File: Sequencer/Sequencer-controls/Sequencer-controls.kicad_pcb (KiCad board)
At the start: 2 copper layers, 163.5 x 105.5 mm, 97 parts, among them SW1 SW_Push_DPDT, SW10 SW_SPDT, SW11 SW_SPDT, SW12 SW_SPDT, SW13 SW_SPDT, SW14 SW_SPDT, SW15 SW_SPDT, SW16 SW_SPDT, SW17 SW_SPDT, SW18 SW_SPDT, SW19 SW_SPDT, SW4 SW_SPDT, SW5 SW_SPDT, SW6 SW_SPDT, SW7 SW_SPDT, SW8 SW_SPDT, SW9 SW_SPDT

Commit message: just playing around
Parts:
- D  : renamed from D3
- moved D   23.8 mm to (9.00, 9.00), turned to -90 degrees
- moved D2 23.8 mm to (3.50, 20.0)
- moved RV_FINE1 23.8 mm to (9.00, 35.0)
- moved SW4 23.8 mm to (9.00, 20.0)
- moved RV_COARSE1 23.7 mm to (9.00, 50.0)
- moved RV_COARSE2 23.4 mm to (23.0, 50.0)
- moved D5 22.2 mm to (25.0, 9.00), turned to -90 degrees
- moved D4 22.0 mm to (19.5, 20.0)
- moved RV_FINE2 22.0 mm to (25.0, 35.0)
- moved SW5 22.0 mm to (25.0, 20.0)
- moved D7 20.6 mm to (41.0, 9.00), turned to -90 degrees
- moved D6 20.2 mm to (35.5, 20.0)
- moved RV_FINE3 20.2 mm to (41.0, 35.0)
- moved SW6 20.2 mm to (41.0, 20.0)
- moved RV_COARSE3 20.2 mm to (41.0, 50.0)
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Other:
- board size 163.5 x 105.5 mm -> 180 x 116.5 mm

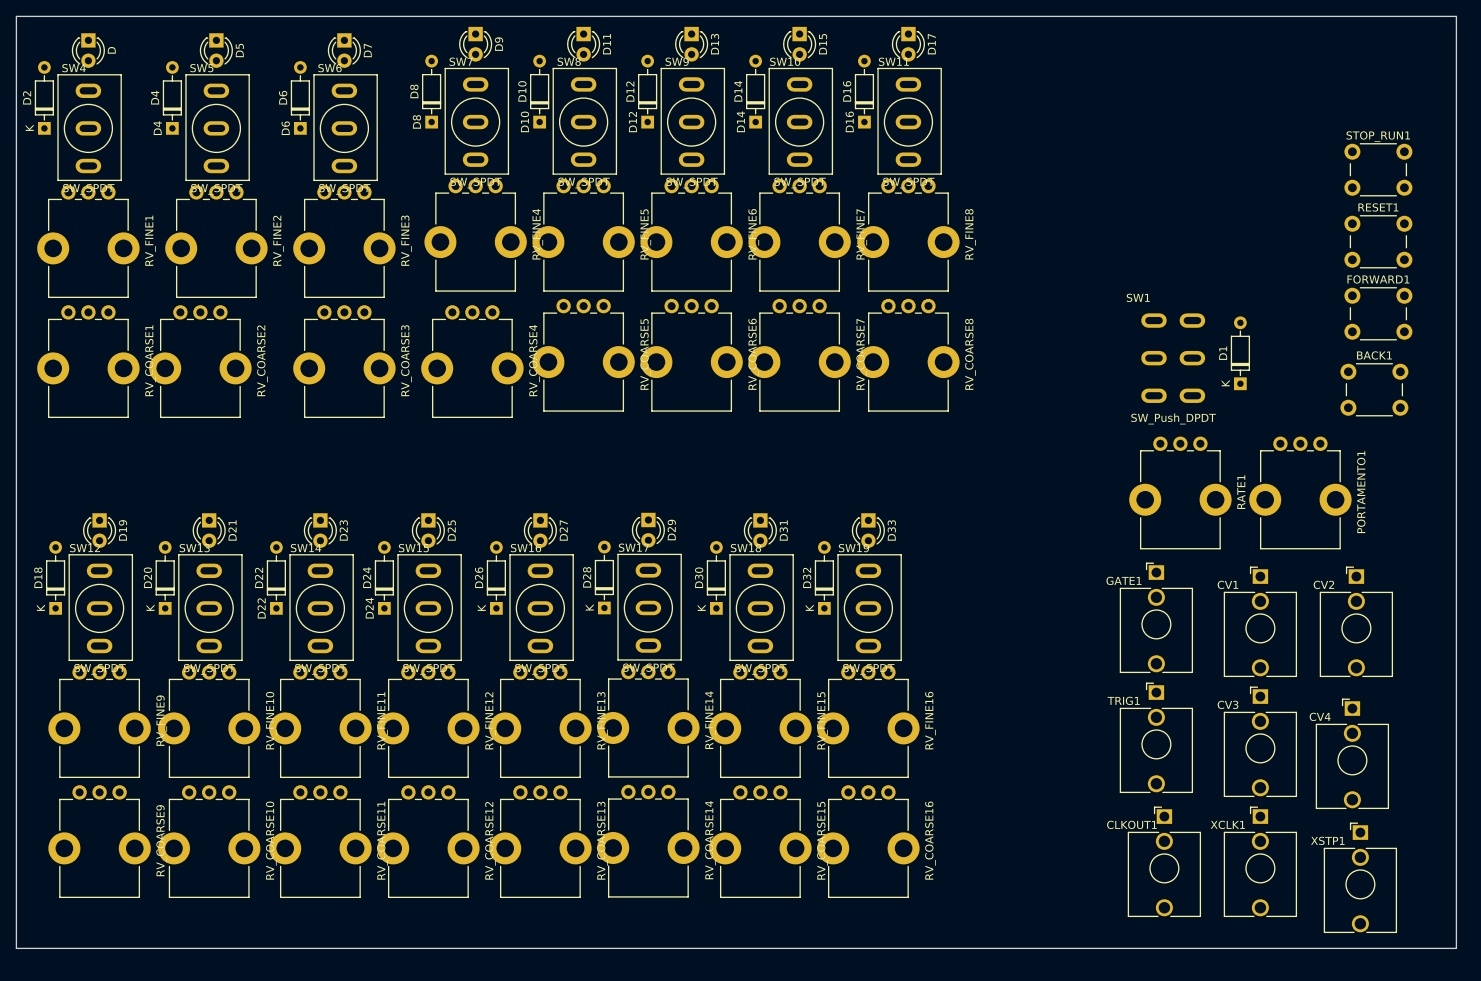
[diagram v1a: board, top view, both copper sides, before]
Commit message: adding connectors to sequencer
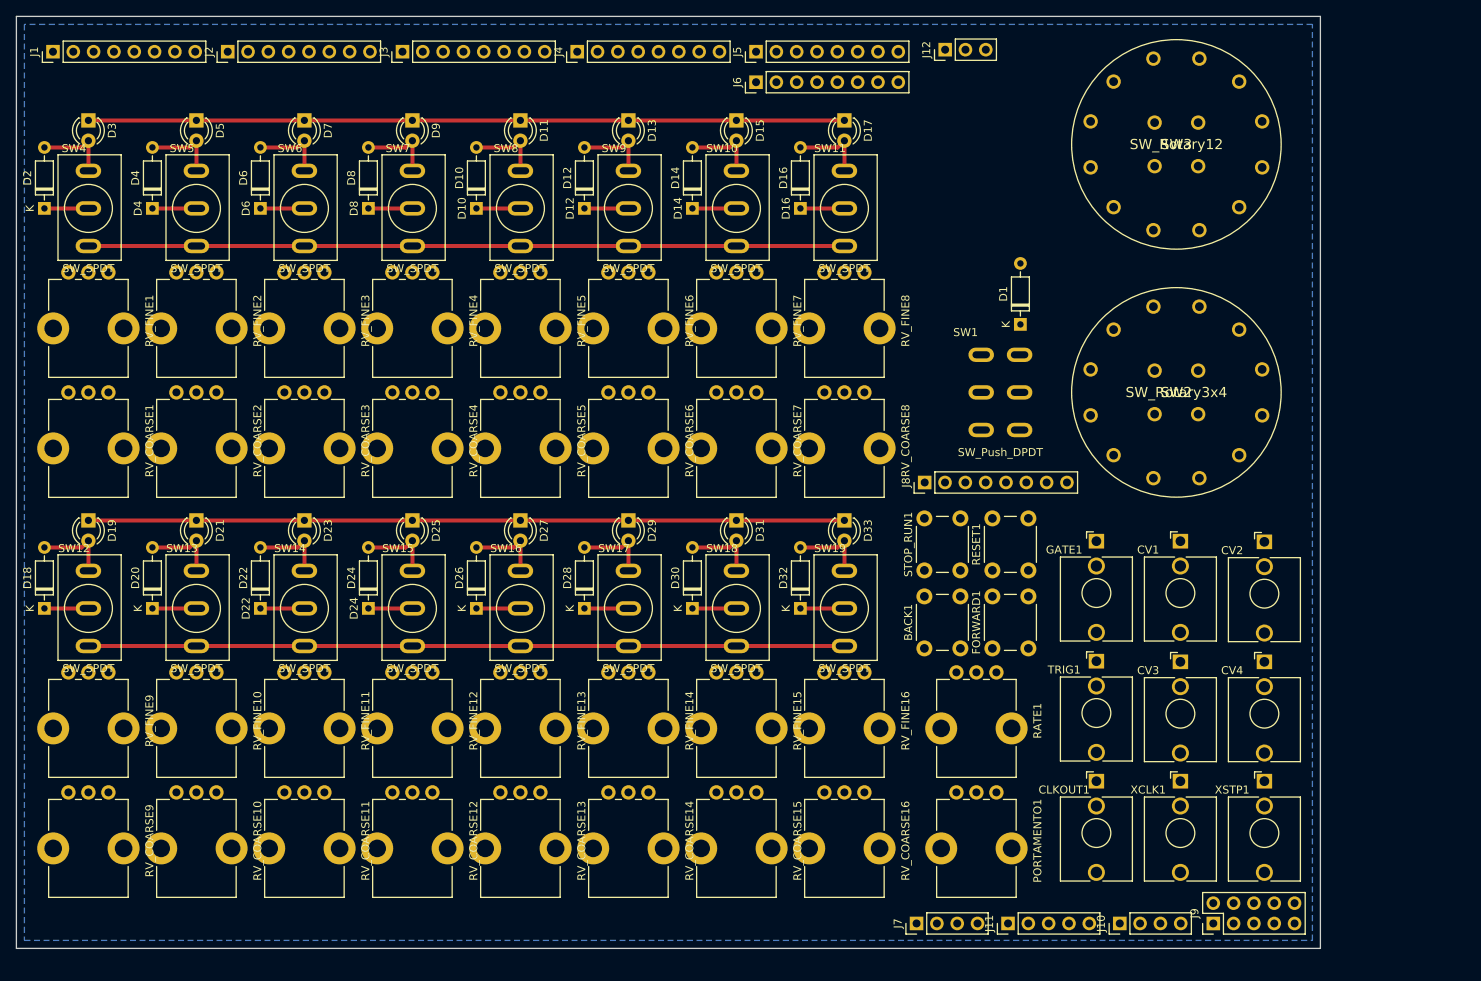
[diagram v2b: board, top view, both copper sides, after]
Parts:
- added J1: Conn_01x08, Connector_PinHeader_2.54mm:PinHeader_1x08_P2.54mm_Vertical, F.Cu at (4.57, 10.4)
- added J10: Conn_01x04, Connector_PinHeader_2.54mm:PinHeader_1x04_P2.54mm_Vertical, F.Cu at (137.9, 119.4)
- added J11: Conn_01x05, Connector_PinHeader_2.54mm:PinHeader_1x05_P2.54mm_Vertical, F.Cu at (124.0, 119.4)
- added J12: Conn_01x03, Connector_PinHeader_2.54mm:PinHeader_1x03_P2.54mm_Vertical, F.Cu at (116.1, 10.2)
- added J2: Conn_01x08, Connector_PinHeader_2.54mm:PinHeader_1x08_P2.54mm_Vertical, F.Cu at (26.4, 10.4)
- added J3: Conn_01x08, Connector_PinHeader_2.54mm:PinHeader_1x08_P2.54mm_Vertical, F.Cu at (48.3, 10.4)
- added J4: Conn_01x08, Connector_PinHeader_2.54mm:PinHeader_1x08_P2.54mm_Vertical, F.Cu at (70.1, 10.4)
- added J5: Conn_01x08, Connector_PinHeader_2.54mm:PinHeader_1x08_P2.54mm_Vertical, F.Cu at (92.5, 10.4)
- added J6: Conn_01x08, Connector_PinHeader_2.54mm:PinHeader_1x08_P2.54mm_Vertical, F.Cu at (92.5, 14.2)
- added J7: Conn_01x04, Connector_PinHeader_2.54mm:PinHeader_1x04_P2.54mm_Vertical, F.Cu at (112.5, 119.4)
- added J8: Conn_01x08, Connector_PinHeader_2.54mm:PinHeader_1x08_P2.54mm_Vertical, F.Cu at (113.5, 64.3)
- added J9: Conn_02x05_Counter_Clockwise, Connector_PinHeader_2.54mm:PinHeader_2x05_P2.54mm_Vertical, F.Cu at (149.6, 119.4)
- added SW2: SW_Rotary3x4, Library:rotary_switch_1P12T, F.Cu at (145.0, 53.0)
- added SW3: SW_Rotary12, Library:rotary_switch_1P12T, F.Cu at (145.0, 22.0)
- D3: renamed from D  
- moved STOP_RUN1 74.8 mm to (113.5, 75.2), turned to 90 degrees
- moved BACK1 63.3 mm to (113.5, 85.0), turned to 90 degrees
- moved FORWARD1 63.0 mm to (122.0, 85.0), turned to 90 degrees
- moved RESET1 62.5 mm to (122.0, 75.2), turned to 90 degrees
- moved PORTAMENTO1 59.5 mm to (120.0, 110.0)
- moved RATE1 38.3 mm to (120.0, 95.0)
- moved D1 28.5 mm to (125.5, 44.5)
- moved SW1 22.0 mm to (123.0, 53.0)
- moved XSTP1 13.6 mm to (156.0, 108.1)
- moved D16 13.4 mm to (98.0, 30.0)
- moved D17 13.4 mm to (103.5, 19.0)
- moved RV_COARSE8 13.4 mm to (103.5, 60.0)
- moved RV_FINE8 13.4 mm to (103.5, 45.0)
- moved SW11 13.4 mm to (103.5, 30.0)
- moved D8 13.4 mm to (44.0, 30.0)
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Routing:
- net GB: track 0.00 -> 189.0 mm
- net CBUS: track 0.00 -> 189.0 mm
- net S7: track 0.00 -> 9.61 mm
- net S5: track 0.00 -> 9.61 mm
- net S4: track 0.00 -> 9.61 mm
- net S3: track 0.00 -> 9.61 mm
- net S2: track 0.00 -> 9.61 mm
- net S1: track 0.00 -> 9.61 mm
- net S8: track 0.00 -> 9.61 mm
- net S6: track 0.00 -> 9.61 mm
- net S9: track 0.00 -> 9.61 mm
- net S10: track 0.00 -> 9.61 mm
- net S16: track 0.00 -> 9.61 mm
- net S15: track 0.00 -> 9.61 mm
- net S14: track 0.00 -> 9.61 mm
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- added copper zone on B.Cu, net GND
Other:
- board size 180 x 116.5 mm -> 163 x 116.5 mm

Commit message: Sequencer control fully routed
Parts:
- added H1: MountingHole_Pad, MountingHole:MountingHole_3.2mm_M3_Pad, F.Cu at (157.0, 37.5)
- added H2: MountingHole_Pad, MountingHole:MountingHole_3.2mm_M3_Pad, F.Cu at (105.0, 118.5)
- added H3: MountingHole_Pad, MountingHole:MountingHole_3.2mm_M3_Pad, F.Cu at (4.00, 118.6)
- SW2: footprint Library:rotary_switch_1P12T -> Library:rotary_switch_3P4T
- renumbered J8 to J10, J12 to J11, J9 to J12, J10 to J7, J11 to J8, J7 to J9
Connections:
- J12 pad 10: +12V -> -12V
- J12 pad 2: GND -> +12V
- J12 pad 5: -12V -> GND
- J12 pad 6: -12V -> GND
- J12 pad 9: GND -> -12V
- PORTAMENTO1 pad : (no net) -> GND
- RATE1 pad : (no net) -> GND
- RV_COARSE1 pad : (no net) -> GND
- RV_COARSE10 pad : (no net) -> GND
- RV_COARSE11 pad : (no net) -> GND
- RV_COARSE12 pad : (no net) -> GND
- RV_COARSE13 pad : (no net) -> GND
- RV_COARSE14 pad : (no net) -> GND
- RV_COARSE15 pad : (no net) -> GND
- RV_COARSE16 pad : (no net) -> GND
- RV_COARSE2 pad : (no net) -> GND
- RV_COARSE3 pad : (no net) -> GND
- RV_COARSE4 pad : (no net) -> GND
- RV_COARSE5 pad : (no net) -> GND
- RV_COARSE6 pad : (no net) -> GND
- RV_COARSE7 pad : (no net) -> GND
- RV_COARSE8 pad : (no net) -> GND
- RV_COARSE9 pad : (no net) -> GND
- RV_FINE1 pad : (no net) -> GND
- RV_FINE10 pad : (no net) -> GND
- RV_FINE11 pad : (no net) -> GND
- RV_FINE12 pad : (no net) -> GND
- RV_FINE13 pad : (no net) -> GND
- RV_FINE14 pad : (no net) -> GND
- RV_FINE15 pad : (no net) -> GND
- RV_FINE16 pad : (no net) -> GND
- RV_FINE2 pad : (no net) -> GND
- RV_FINE3 pad : (no net) -> GND
- RV_FINE4 pad : (no net) -> GND
- RV_FINE5 pad : (no net) -> GND
- RV_FINE6 pad : (no net) -> GND
- RV_FINE7 pad : (no net) -> GND
- RV_FINE8 pad : (no net) -> GND
- RV_FINE9 pad : (no net) -> GND
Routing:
- net VSRC: track 0.00 -> 520.5 mm
- net S9: track 9.61 -> 212.6 mm, vias 0 -> 1
- net S11: track 9.61 -> 192.0 mm, vias 0 -> 1
- net C11: track 0.00 -> 178.9 mm, vias 0 -> 1
- net S14: track 9.61 -> 184.0 mm
- net S12: track 9.61 -> 183.9 mm, vias 0 -> 1
- net S10: track 9.61 -> 178.4 mm, vias 0 -> 1
- net S13: track 9.61 -> 164.7 mm, vias 0 -> 2
- net C9: track 0.00 -> 146.3 mm
- net S15: track 9.61 -> 149.8 mm, vias 0 -> 1
- net F9: track 0.00 -> 128.3 mm
- net S4: track 9.61 -> 136.9 mm
- net C12: track 0.00 -> 117.9 mm, vias 0 -> 1
- net S5: track 9.61 -> 125.8 mm, vias 0 -> 1
- net S6: track 9.61 -> 120.7 mm, vias 0 -> 1
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- added copper zone on F.Cu, net GND
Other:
- board text added: "+12V"
- board text added: "-12V"
- board text added: "C1"
- board text added: "C10"
- board text added: "C11"
- board text added: "C12"
- board text added: "C13"
- board text added: "C14"
- board text added: "C15"
- board text added: "C16"
- board text added: "C2"
- board text added: "C3"
- board text added: "C4"
- board text added: "C5"
- board text added: "C6"
- board text added: "C7"
- board text added: "C8"
- board text added: "C9"
- board text added: "CBUS"
- board text added: "CLKOUT"
- board text added: "CV1"
- board text added: "CV2"
- board text added: "CV3"
- board text added: "F1"
- board text added: "F10"
- board text added: "F11"
- board text added: "F12"
- board text added: "F13"
- board text added: "F14"
- board text added: "F15"
- board text added: "F16"
- board text added: "F2"
- board text added: "F3"
- board text added: "F4"
- board text added: "F5"
- board text added: "F6"
- board text added: "F7"
- board text added: "F8"
- board text added: "F9"
- board text added: "GATE"
- board text added: "GB"
- board text added: "GND"
- board text added: "PORT_1_2"
- board text added: "PORT_3"
- board text added: "RATE_1_2"
- board text added: "RATE_3"
- board text added: "S1"
- board text added: "S16"
- board text added: "S8"
- board text added: "S9"
- board text added: "TRIG"
- board text added: "VSRC"
- board text added: "XCLK"
- board text added: "XSTP"

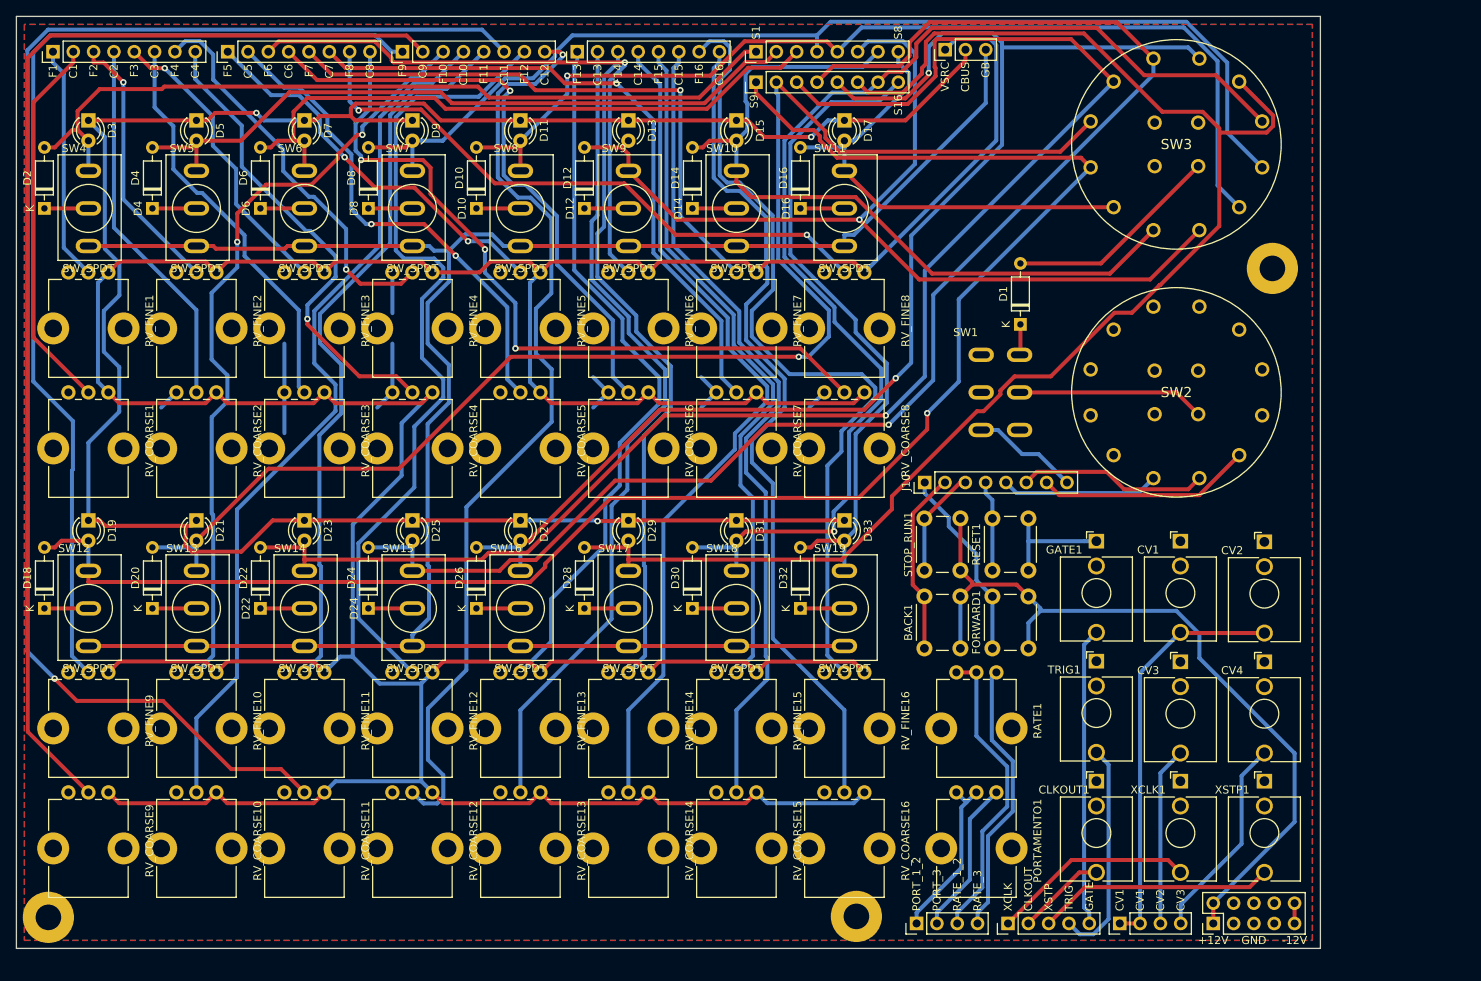
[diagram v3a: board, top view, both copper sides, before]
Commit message: moved to 4 layers
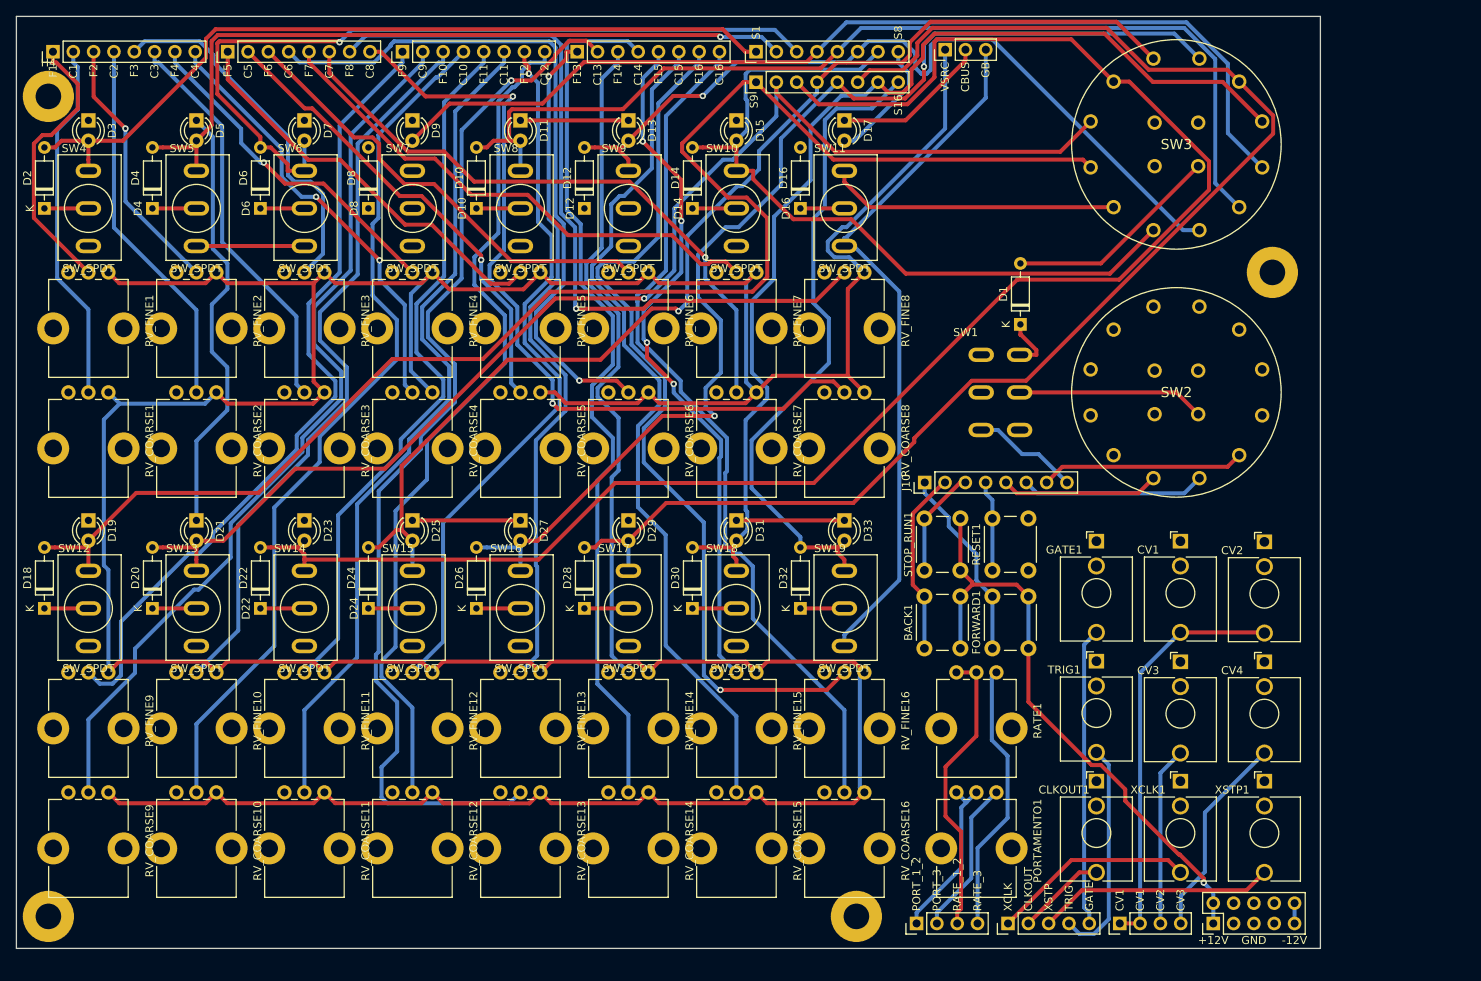
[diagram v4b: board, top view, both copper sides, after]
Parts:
- added H4: MountingHole_Pad, MountingHole:MountingHole_3.2mm_M3_Pad, F.Cu at (4.00, 16.0)
- moved H1 0.50 mm to (157.0, 38.0)
- moved H3 0.12 mm to (4.00, 118.5)
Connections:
- PORTAMENTO1 pad : GND -> (no net)
- RATE1 pad : GND -> (no net)
- RV_COARSE1 pad : GND -> (no net)
- RV_COARSE10 pad : GND -> (no net)
- RV_COARSE11 pad : GND -> (no net)
- RV_COARSE12 pad : GND -> (no net)
- RV_COARSE13 pad : GND -> (no net)
- RV_COARSE14 pad : GND -> (no net)
- RV_COARSE15 pad : GND -> (no net)
- RV_COARSE16 pad : GND -> (no net)
- RV_COARSE2 pad : GND -> (no net)
- RV_COARSE3 pad : GND -> (no net)
- RV_COARSE4 pad : GND -> (no net)
- RV_COARSE5 pad : GND -> (no net)
- RV_COARSE6 pad : GND -> (no net)
- RV_COARSE7 pad : GND -> (no net)
- RV_COARSE8 pad : GND -> (no net)
- RV_COARSE9 pad : GND -> (no net)
- RV_FINE1 pad : GND -> (no net)
- RV_FINE10 pad : GND -> (no net)
- RV_FINE11 pad : GND -> (no net)
- RV_FINE12 pad : GND -> (no net)
- RV_FINE13 pad : GND -> (no net)
- RV_FINE14 pad : GND -> (no net)
- RV_FINE15 pad : GND -> (no net)
- RV_FINE16 pad : GND -> (no net)
- RV_FINE2 pad : GND -> (no net)
- RV_FINE3 pad : GND -> (no net)
- RV_FINE4 pad : GND -> (no net)
- RV_FINE5 pad : GND -> (no net)
- RV_FINE6 pad : GND -> (no net)
- RV_FINE7 pad : GND -> (no net)
- RV_FINE8 pad : GND -> (no net)
- RV_FINE9 pad : GND -> (no net)
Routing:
- net C11: track 178.9 -> 105.7 mm, vias 1 -> 0
- net GND: track 56.2 -> 0.00 mm
- net S12: track 183.9 -> 145.8 mm
- net C9: track 146.3 -> 113.0 mm
- net C13: track 104.2 -> 133.1 mm, vias 0 -> 1
- net F9: track 128.3 -> 101.1 mm
- net S9: track 212.6 -> 188.9 mm, vias 1 -> 0
- net +12V: track 99.3 -> 76.3 mm, vias 0 -> 1
- net S10: track 178.4 -> 157.8 mm
- net S3: track 80.4 -> 100.5 mm, vias 0 -> 1
- net F8: track 77.0 -> 96.9 mm, vias 2 -> 1
- net S13: track 164.7 -> 145.7 mm
- net S6: track 120.7 -> 101.9 mm
- net CBUS: track 282.5 -> 264.1 mm, vias 3 -> 0
- net S11: track 192.0 -> 209.9 mm, vias 1 -> 0
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- added copper zone on In1.Cu, net GND
- added copper zone on In2.Cu, net GND
- removed copper zone on B.Cu, net GND
- removed copper zone on F.Cu, net GND
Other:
- copper layers 2 -> 4
